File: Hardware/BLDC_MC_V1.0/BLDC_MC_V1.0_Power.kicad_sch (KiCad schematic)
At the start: 52 parts, among them Q7 BSC027N10NS5ATMA1, U1 LM76005RNPR, U16 LM74700QDRQ1, U5 LDL1117S33R, U7 NCV4274ADT50RKG

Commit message: Update board placement
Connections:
- net Buck_SW: now reaches C32.1, L1.1, U1.1 (SW), U1.2 (SW), U1.3 (SW), U1.4 (SW), U1.5 (SW)
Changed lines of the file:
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@@
 	(wire
 		(pts
-			(xy 154.94 45.72) (xy 153.67 45.72)
+			(xy 156.21 43.18) (xy 153.67 43.18)
 		)
 		(stroke
@@
 		(pts
 			(xy 22.86 85.09) (xy 25.4 85.09)
+		)
+		(stroke
+			(width 0)
+			(type default)
+		)
+	)
+	(wire
+		(pts
+			(xy 153.67 43.18) (xy 153.67 45.72)
 		)
 		(stroke
@@
 		)
 	)
-	(label "VCC_Buck"
-		(at 154.94 45.72 0)
+	(label "Buck_SW"
+		(at 156.21 46.99 0)
 		(effects
 			(font
+				(size 1.27 1.27)
+			)
+			(justify left bottom)
+		)
+	)
+	(label "VCC_Buck"
+		(at 156.21 43.18 0)
+		(effects
+			(font

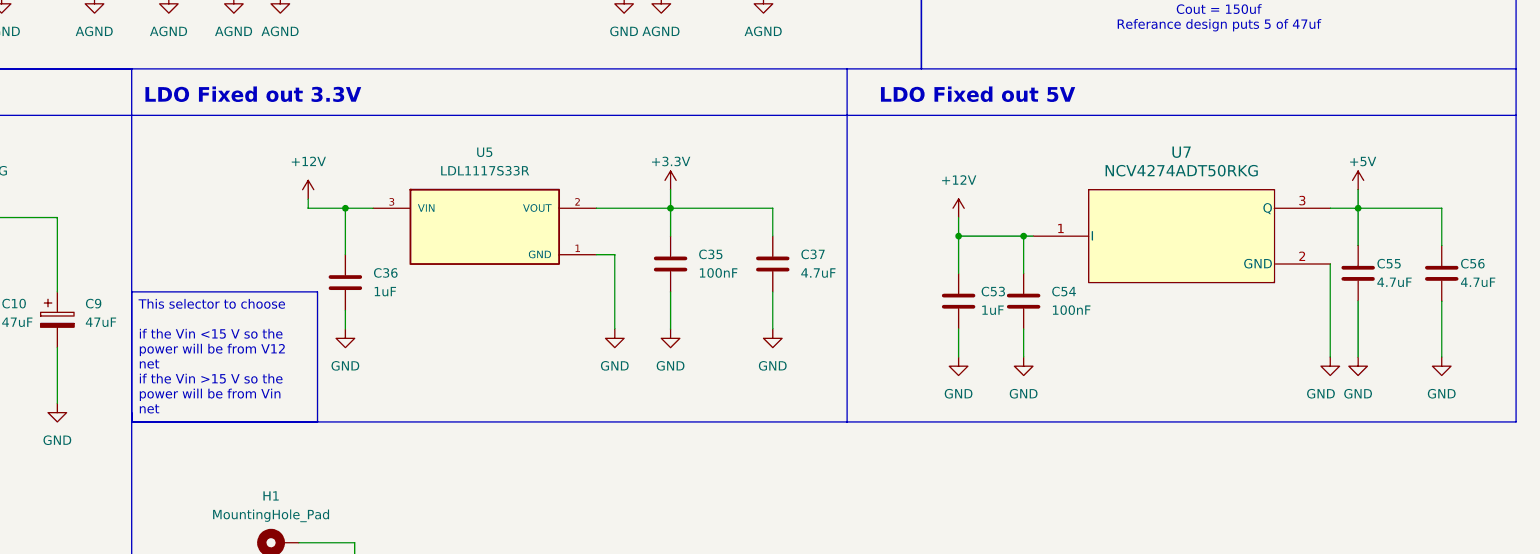
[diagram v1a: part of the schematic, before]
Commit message: Update the layout of the board by routing the connections between controller and gate drive
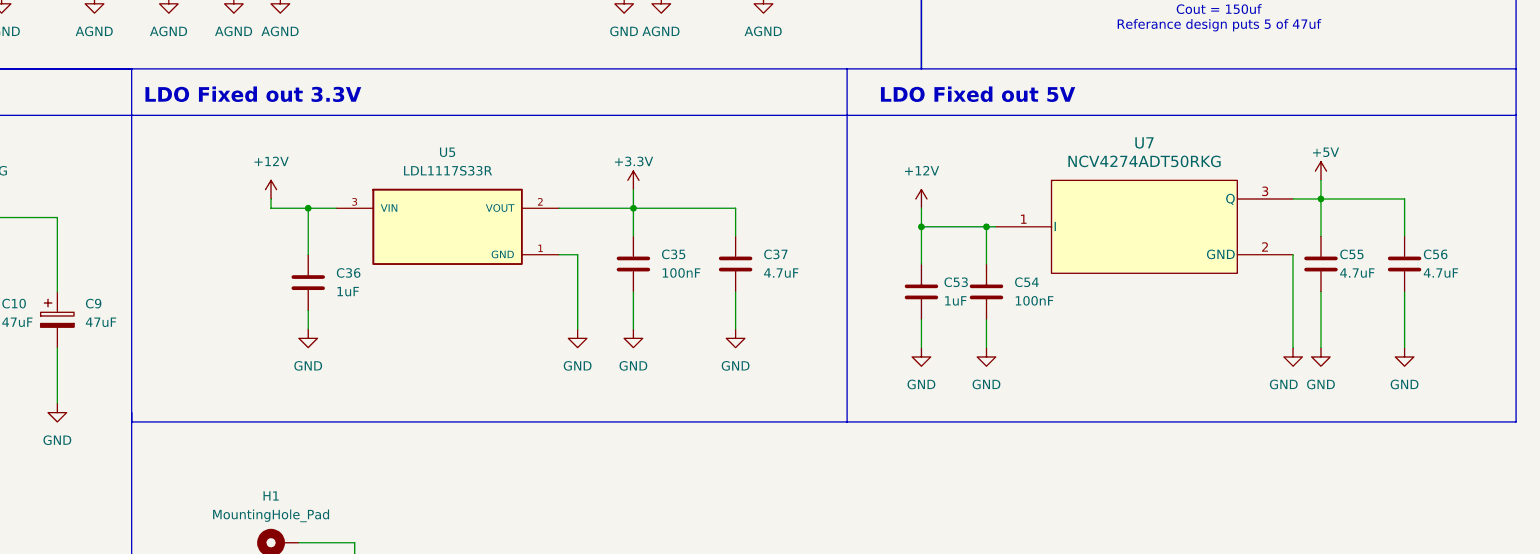
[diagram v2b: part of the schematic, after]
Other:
- moved on the sheet: C35, C36, C37, C53, C54, C55, C56, U5, U7
